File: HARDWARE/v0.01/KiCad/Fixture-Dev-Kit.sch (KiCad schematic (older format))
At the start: 0 parts

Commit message: adding some comments for Howie
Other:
- note added: "- Led Part Number (color, size)\n- confirm LED circuit\n- is 1K resistor correct?"
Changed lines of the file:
@@
 LIBS:contrib
 LIBS:valves
+LIBS:FDN337N
 LIBS:Fixture-Dev-Kit-cache
 EELAYER 25 0
@@
 $Descr A4 11693 8268
 encoding utf-8
-Sheet 1 9
+Sheet 1 10
 Title ""
 Date ""
@@
 $EndSheet
 $Sheet
-S 850  750  2800 2200
+S 850  900  2800 2200
 U 59EE6806
 F0 "Fixture Dev Kit - Functional Computer" 60
@@
 $EndSheet
 $Sheet
-S 6300 5050 1150 800
+S 4350 3850 1150 800
 U 59EFF8A7
-F0 "Fixture Dev Kit - Mosfets" 61
-F1 "FixtureDevKit-Mosfet.sch" 61
+F0 "Fixture Dev Kit - PMosfets" 61
+F1 "FixtureDevKit-PMosfet.sch" 61
 $EndSheet
 $Comp
@@
 Wire Wire Line
 	1300 7350 1300 7450
+Text Notes 8200 4900 0    60   ~ 0
+- Led Part Number (color, size)\n- confirm LED circuit\n- is 1K resistor correct?
+$Sheet
+S 4350 4950 1150 750
+U 59F1138D
+F0 "Fixture Dev Kits - NMosfets" 60
+F1 "FixtureDevKit-NMosfets.sch" 60
+$EndSheet
 $EndSCHEMATC

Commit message: updating the cover page
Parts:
- added J?: POWER, symbol Screw_Terminal_01x02
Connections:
- net labels added: +5V
- net labels removed: VCC
- wire segments 2 -> 5
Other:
- note added: "5V-10A Power Supply\n"
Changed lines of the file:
@@
 $EndDescr
 $Sheet
-S 8100 4550 2400 1200
+S 4050 5300 1700 700
 U 59EE3928
 F0 "Fixture Dev Kit Switches" 60
@@
 $EndSheet
 $Sheet
-S 4750 750  1100 2600
+S 4054 2346 800  1050
 U 59EE50B5
 F0 "Fixture Dev Kit - INA" 60
 F1 "FixtureDevKit-INA.sch" 60
+F2 "I2C-SDA" B T 4704 2346 60
+F3 "I2C-SCK" B T 4554 2346 60
+F4 "C4-VCC-3V3" I T 4254 2346 60
 $EndSheet
 $Sheet
-S 6200 750  1000 2600
+S 5116 2334 784  1066
 U 59EEAF92
 F0 "Fixture Dev Kit - ADS" 60
 F1 "FixtureDevKit-ADS.sch" 60
+F2 "I2C-SDA" B T 5766 2334 60
+F3 "I2C-SCK" B T 5616 2334 60
+F4 "C4-VCC-3V3" I T 5300 2334 60
 $EndSheet
 $Sheet
-S 7700 750  950  2600
+S 4050 3600 800  600
 U 59EE63FB
 F0 "Fixture Dev Kit Dummy Loads" 60
@@
 $EndSheet
 $Sheet
-S 850  900  2800 2200
-U 59EE6806
-F0 "Fixture Dev Kit - Functional Computer" 60
-F1 "FixtureDevKit-Functional-Computer.sch" 60
-$EndSheet
-$Sheet
-S 9300 900  1800 1150
+S 7500 950  1650 1350
 U 59EE1B11
 F0 "Fixture Dev Kit - DUT" 60
@@
 $EndSheet
 $Sheet
-S 6200 3750 1150 850
+S 6205 2345 745  1055
 U 59EF8AA8
 F0 "Fixture Dev Kit - IO Expander" 60
 F1 "FixtureDevKit-IOExpander.sch" 60
+F2 "I2C-SDA" B T 6755 2345 60
+F3 "I2C-SDK" B T 6605 2345 60
+F4 "C4-VCC-4V4" I T 6305 2345 60
 $EndSheet
 $Sheet
-S 4350 3850 1150 800
+S 5850 3600 800  600
 U 59EFF8A7
 F0 "Fixture Dev Kit - PMosfets" 61
@@
 L PWR_FLAG #FLG01
 U 1 1 59EFDEB7
-P 800 7350
-F 0 "#FLG01" H 800 7425 50  0001 C CNN
-F 1 "PWR_FLAG" H 800 7500 50  0000 C CNN
-F 2 "" H 800 7350 50  0001 C CNN
-F 3 "" H 800 7350 50  0001 C CNN
-	1    800  7350
+P 900 7400
+F 0 "#FLG01" H 900 7475 50  0001 C CNN
+F 1 "PWR_FLAG" H 900 7550 50  0000 C CNN
+F 2 "" H 900 7400 50  0001 C CNN
+F 3 "" H 900 7400 50  0001 C CNN
+	1    900  7400
 	1    0    0    -1
 $EndComp
@@
 L PWR_FLAG #FLG02
 U 1 1 59EFDEC9
-P 1300 7350
-F 0 "#FLG02" H 1300 7425 50  0001 C CNN
-F 1 "PWR_FLAG" H 1300 7500 50  0000 C CNN
-F 2 "" H 1300 7350 50  0001 C CNN
-F 3 "" H 1300 7350 50  0001 C CNN
-	1    1300 7350
+P 1400 7400
+F 0 "#FLG02" H 1400 7475 50  0001 C CNN
+F 1 "PWR_FLAG" H 1400 7550 50  0000 C CNN
+F 2 "" H 1400 7400 50  0001 C CNN
+F 3 "" H 1400 7400 50  0001 C CNN
+	1    1400 7400
 	1    0    0    -1
 $EndComp
@@
 L GND #PWR03
 U 1 1 59EFDED6
-P 1300 7450
-F 0 "#PWR03" H 1300 7200 50  0001 C CNN
-F 1 "GND" H 1300 7300 50  0000 C CNN
-F 2 "" H 1300 7450 50  0001 C CNN
-F 3 "" H 1300 7450 50  0001 C CNN
-	1    1300 7450
+P 1400 7500
+F 0 "#PWR03" H 1400 7250 50  0001 C CNN
+F 1 "GND" H 1400 7350 50  0000 C CNN
+F 2 "" H 1400 7500 50  0001 C CNN
+F 3 "" H 1400 7500 50  0001 C CNN
+	1    1400 7500
 	1    0    0    -1
 $EndComp
-$Comp
-L VCC #PWR04
-U 1 1 59EFDEEA
-P 800 7450
-F 0 "#PWR04" H 800 7300 50  0001 C CNN
-F 1 "VCC" H 800 7600 50  0000 C CNN
-F 2 "" H 800 7450 50  0001 C CNN
-F 3 "" H 800 7450 50  0001 C CNN
-	1    800  7450
-	-1   0    0    1
-$EndComp
 Wire Wire Line
-	800  7350 800  7450
+	900  7400 900  7500
 Wire Wire Line
-	1300 7350 1300 7450
-Text Notes 8200 4900 0    60   ~ 0
-- Led Part Number (color, size)\n- confirm LED circuit\n- is 1K resistor correct?
+	1400 7400 1400 7500
 $Sheet
-S 4350 4950 1150 750
+S 5850 4500 800  600
 U 59F1138D
 F0 "Fixture Dev Kits - NMosfets" 60
 F1 "FixtureDevKit-NMosfets.sch" 60
 $EndSheet
+$Comp
+L Screw_Terminal_01x02 J?
+U 1 1 59F1B009
+P 1050 6850
+F 0 "J?" H 1050 6950 50  0000 C CNN
+F 1 "POWER" H 1050 6650 50  0000 C CNN
+F 2 "" H 1050 6850 50  0001 C CNN
+F 3 "" H 1050 6850 50  0001 C CNN
+	1    1050 6850
+	-1   0    0    1
+$EndComp
+Wire Wire Line
+	1250 6750 1500 6750
+$Comp
+L GND #PWR?
+U 1 1 59F1B0B1
+P 1500 6850
+F 0 "#PWR?" H 1500 6600 50  0001 C CNN
+F 1 "GND" H 1500 6700 50  0000 C CNN
+F 2 "" H 1500 6850 50  0001 C CNN
+F 3 "" H 1500 6850 50  0001 C CNN
+	1    1500 6850
+	1    0    0    -1
+$EndComp
+Wire Wire Line
+	1250 6850 1500 6850
+Text Notes 600  6350 0    98   ~ 0
+5V-10A Power Supply\n
+Wire Notes Line
+	550  6150 2250 6150
+Wire Notes Line
+	2250 6150 2250 7150
+Wire Notes Line
+	2250 7150 550  7150
+Wire Notes Line
+	550  7150 550  6150
+Wire Notes Line
+	550  6400 2250 6400
+$Comp
+L +5V #PWR?
+U 1 1 59F1DD6A
+P 900 7500
+F 0 "#PWR?" H 900 7350 50  0001 C CNN
+F 1 "+5V" H 900 7640 50  0000 C CNN
+F 2 "" H 900 7500 50  0001 C CNN
+F 3 "" H 900 7500 50  0001 C CNN
+	1    900  7500
+	-1   0    0    1
+$EndComp
+$Comp
+L +5V #PWR?
+U 1 1 59F1DD81
+P 1500 6750
+F 0 "#PWR?" H 1500 6600 50  0001 C CNN
+F 1 "+5V" H 1500 6890 50  0000 C CNN
+F 2 "" H 1500 6750 50  0001 C CNN
+F 3 "" H 1500 6750 50  0001 C CNN
+	1    1500 6750
+	1    0    0    -1
+$EndComp
+$Sheet
+S 1500 950  1650 1350
+U 59EE6806
+F0 "Fixture Dev Kit - Functional Computer" 60
+F1 "FixtureDevKit-Functional-Computer.sch" 60
+F2 "I2C-SDA" B R 3150 1150 60
+F3 "I2C-SCK" B R 3150 1250 60
+F4 "+5V" I R 3150 1600 60
+F5 "C4-VCC-5V" O R 3150 1900 60
+F6 "C4-VCC-3V3" O R 3150 2050 60
+$EndSheet
+$Comp
+L +5V #PWR?
+U 1 1 59F2758A
+P 3300 1600
+F 0 "#PWR?" H 3300 1450 50  0001 C CNN
+F 1 "+5V" H 3300 1740 50  0000 C CNN
+F 2 "" H 3300 1600 50  0001 C CNN
+F 3 "" H 3300 1600 50  0001 C CNN
+	1    3300 1600
+	0    1    1    0
+$EndComp
+Wire Wire Line
+	3300 1600 3150 1600
+Text Notes 4100 5650 0    60   ~ 0
+- Led Part Number (color, size)\n- confirm LED circuit\n- is 1K resistor correct?
 $EndSCHEMATC

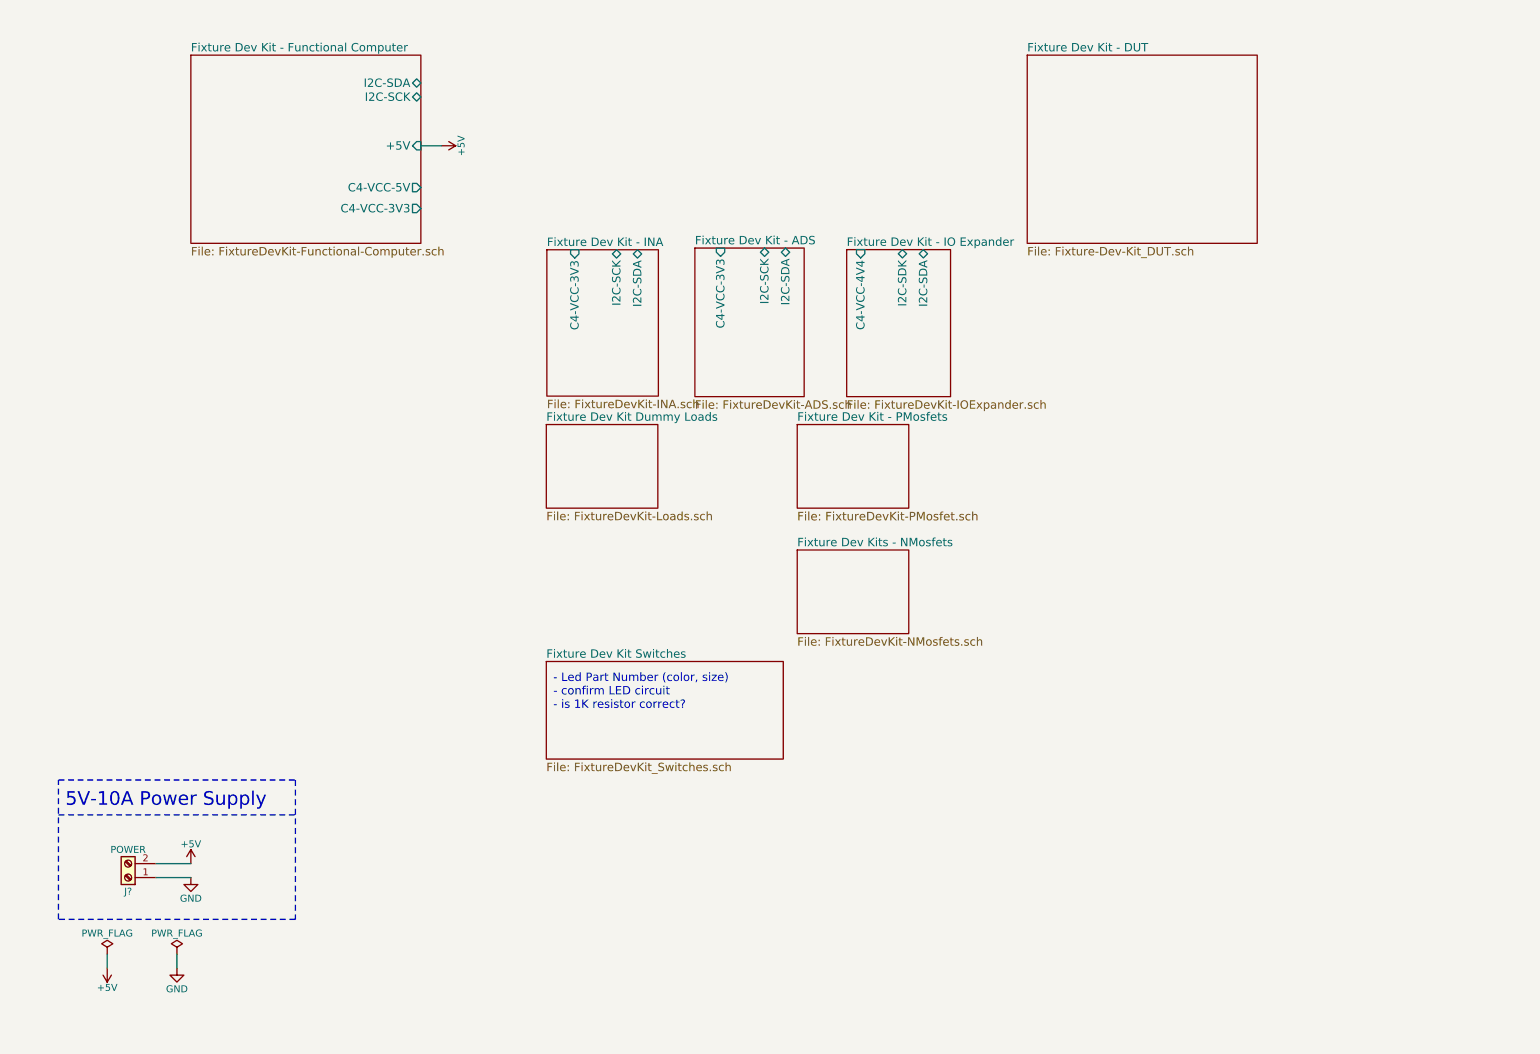
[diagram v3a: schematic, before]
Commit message: adjusting page sizes and cleaning up schematics
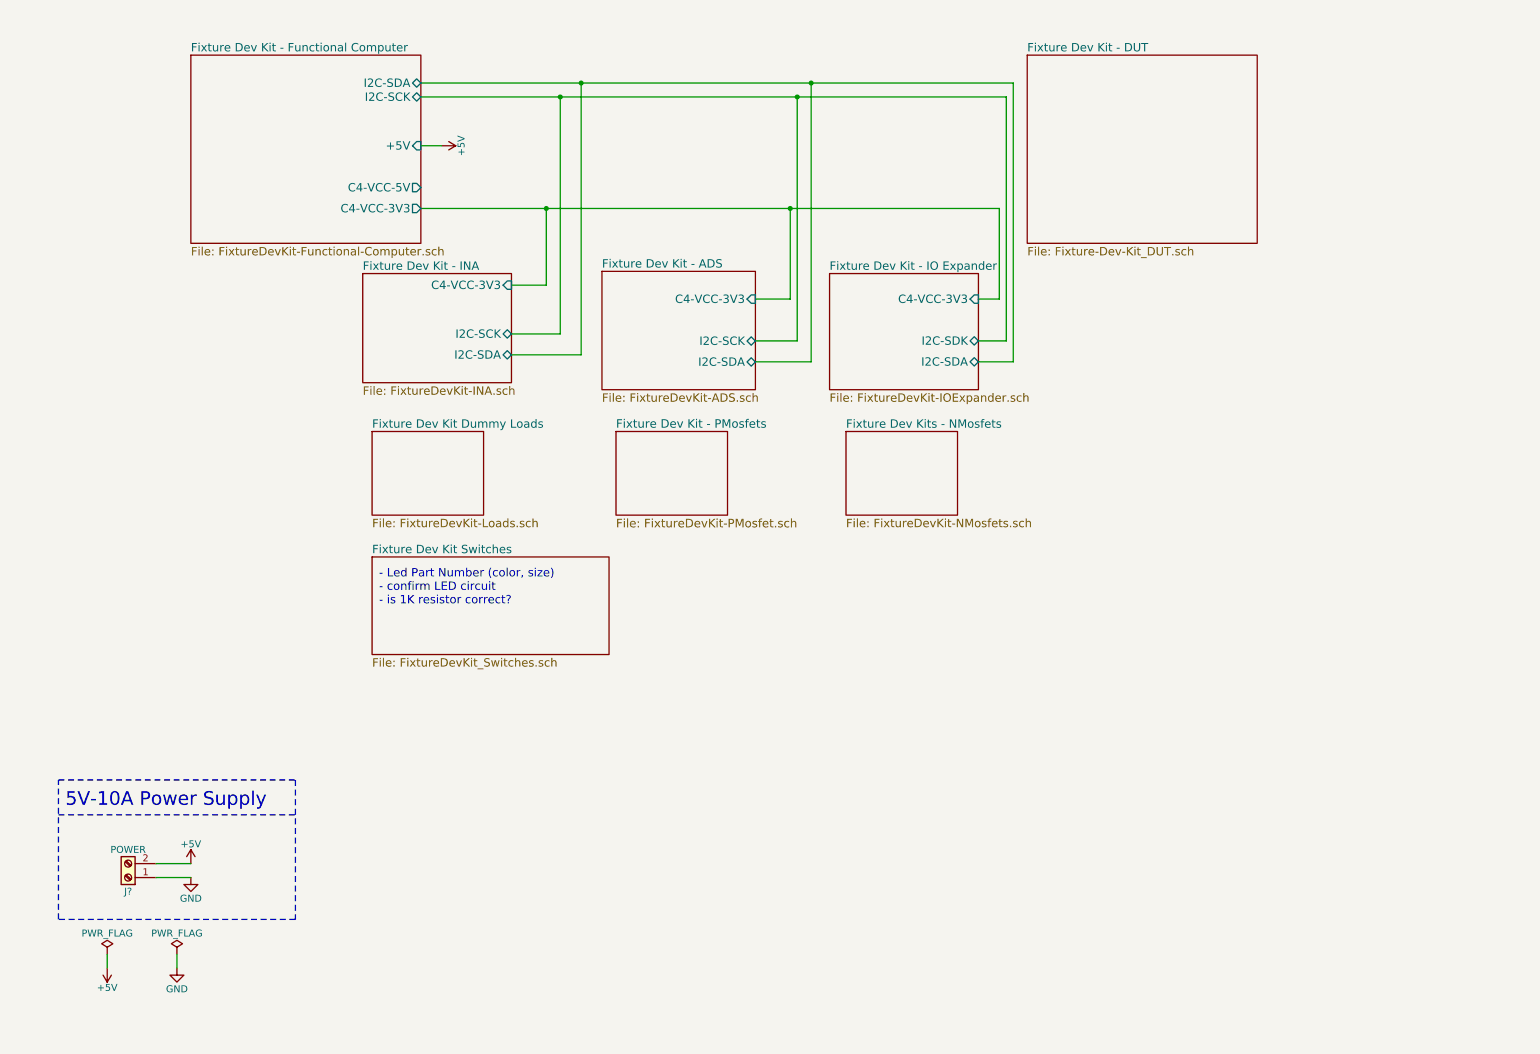
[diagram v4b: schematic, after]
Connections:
- wire segments 5 -> 26
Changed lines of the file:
@@
 EELAYER 25 0
 EELAYER END
-$Descr A4 11693 8268
+$Descr USLetter 11000 8500
 encoding utf-8
 Sheet 1 10
@@
 $EndDescr
 $Sheet
-S 4050 5300 1700 700
+S 2800 4550 1700 700
 U 59EE3928
 F0 "Fixture Dev Kit Switches" 60
@@
 $EndSheet
 $Sheet
-S 4054 2346 800  1050
-U 59EE50B5
-F0 "Fixture Dev Kit - INA" 60
-F1 "FixtureDevKit-INA.sch" 60
-F2 "I2C-SDA" B T 4704 2346 60
-F3 "I2C-SCK" B T 4554 2346 60
-F4 "C4-VCC-3V3" I T 4254 2346 60
-$EndSheet
-$Sheet
-S 5116 2334 784  1066
+S 4449 2501 1101 849
 U 59EEAF92
 F0 "Fixture Dev Kit - ADS" 60
 F1 "FixtureDevKit-ADS.sch" 60
-F2 "I2C-SDA" B T 5766 2334 60
-F3 "I2C-SCK" B T 5616 2334 60
-F4 "C4-VCC-3V3" I T 5300 2334 60
-$EndSheet
-$Sheet
-S 4050 3600 800  600
+F2 "I2C-SDA" B R 5550 3151 60
+F3 "I2C-SCK" B R 5550 3001 60
+F4 "C4-VCC-3V3" I R 5550 2700 60
+$EndSheet
+$Sheet
+S 2800 3650 800  600
 U 59EE63FB
 F0 "Fixture Dev Kit Dummy Loads" 60
@@
 $EndSheet
 $Sheet
-S 6205 2345 745  1055
+S 6082 2517 1068 833
 U 59EF8AA8
 F0 "Fixture Dev Kit - IO Expander" 60
 F1 "FixtureDevKit-IOExpander.sch" 60
-F2 "I2C-SDA" B T 6755 2345 60
-F3 "I2C-SDK" B T 6605 2345 60
-F4 "C4-VCC-4V4" I T 6305 2345 60
-$EndSheet
-$Sheet
-S 5850 3600 800  600
+F2 "I2C-SDA" B R 7150 3150 60
+F3 "I2C-SDK" B R 7150 3000 60
+F4 "C4-VCC-3V3" I R 7150 2700 60
+$EndSheet
+$Sheet
+S 4550 3650 800  600
 U 59EFF8A7
 F0 "Fixture Dev Kit - PMosfets" 61
@@
 	1400 7400 1400 7500
 $Sheet
-S 5850 4500 800  600
+S 6200 3650 800  600
 U 59F1138D
 F0 "Fixture Dev Kits - NMosfets" 60
@@
 Wire Wire Line
 	3300 1600 3150 1600
-Text Notes 4100 5650 0    60   ~ 0
+Text Notes 2850 4900 0    60   ~ 0
 - Led Part Number (color, size)\n- confirm LED circuit\n- is 1K resistor correct?
+$Sheet
+S 2733 2517 1067 783
+U 59EE50B5
+F0 "Fixture Dev Kit - INA" 60
+F1 "FixtureDevKit-INA.sch" 60
+F2 "I2C-SDA" B R 3800 3100 60
+F3 "I2C-SCK" B R 3800 2950 60
+F4 "C4-VCC-3V3" I R 3800 2600 60
+$EndSheet
+Wire Wire Line
+	3800 2600 4050 2600
+Wire Wire Line
+	4050 2600 4050 2050
+Wire Wire Line
+	3150 2050 7300 2050
+Wire Wire Line
+	3800 2950 4150 2950
+Wire Wire Line
+	4150 2950 4150 1250
+Wire Wire Line
+	3150 1250 7350 1250
+Wire Wire Line
+	3800 3100 4300 3100
+Wire Wire Line
+	4300 3100 4300 1150
+Wire Wire Line
+	3150 1150 7400 1150
+Wire Wire Line
+	5800 2050 5800 2700
+Wire Wire Line
+	5800 2700 5550 2700
+Connection ~ 4050 2050
+Wire Wire Line
+	5550 3000 5850 3000
+Wire Wire Line
+	5850 3000 5850 1250
+Connection ~ 4150 1250
+Wire Wire Line
+	5550 3150 5950 3150
+Wire Wire Line
+	5950 3150 5950 1150
+Connection ~ 4300 1150
+Wire Wire Line
+	7300 2050 7300 2700
+Wire Wire Line
+	7300 2700 7150 2700
+Connection ~ 5800 2050
+Wire Wire Line
+	7150 3000 7350 3000
+Wire Wire Line
+	7350 3000 7350 1250
+Connection ~ 5850 1250
+Wire Wire Line
+	7150 3150 7400 3150
+Wire Wire Line
+	7400 3150 7400 1150
+Connection ~ 5950 1150
 $EndSCHEMATC

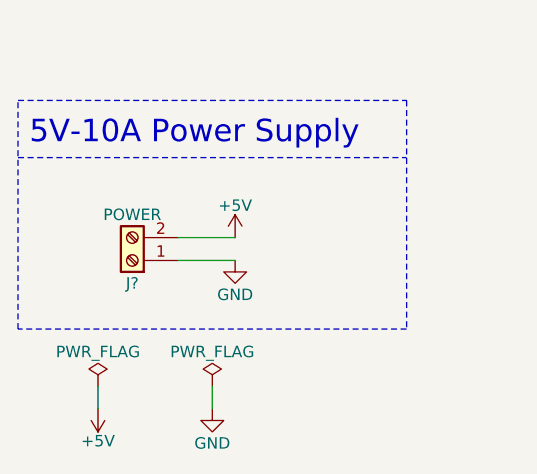
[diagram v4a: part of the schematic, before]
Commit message: cleaning up schematic, run rules check, generate net list
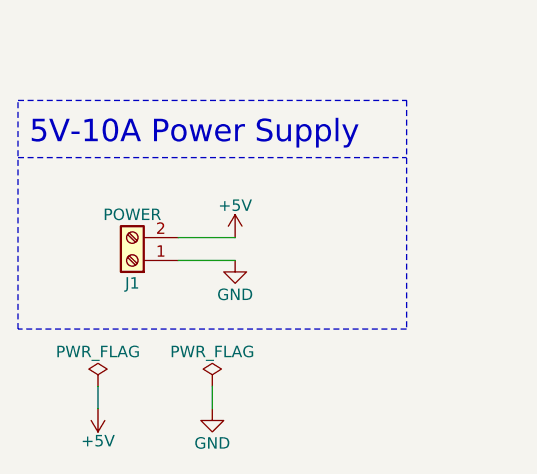
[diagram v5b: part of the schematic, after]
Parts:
- gave numbers to parts that had none: 1
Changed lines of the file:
@@
 $EndSheet
 $Comp
-L Screw_Terminal_01x02 J?
+L Screw_Terminal_01x02 J1
 U 1 1 59F1B009
 P 1050 6850
-F 0 "J?" H 1050 6950 50  0000 C CNN
+F 0 "J1" H 1050 6950 50  0000 C CNN
 F 1 "POWER" H 1050 6650 50  0000 C CNN
 F 2 "" H 1050 6850 50  0001 C CNN
@@
 	1250 6750 1500 6750
 $Comp
-L GND #PWR?
+L GND #PWR04
 U 1 1 59F1B0B1
 P 1500 6850
-F 0 "#PWR?" H 1500 6600 50  0001 C CNN
+F 0 "#PWR04" H 1500 6600 50  0001 C CNN
 F 1 "GND" H 1500 6700 50  0000 C CNN
 F 2 "" H 1500 6850 50  0001 C CNN
@@
 	550  6400 2250 6400
 $Comp
-L +5V #PWR?
+L +5V #PWR05
 U 1 1 59F1DD6A
 P 900 7500
-F 0 "#PWR?" H 900 7350 50  0001 C CNN
+F 0 "#PWR05" H 900 7350 50  0001 C CNN
 F 1 "+5V" H 900 7640 50  0000 C CNN
 F 2 "" H 900 7500 50  0001 C CNN
@@
 $EndComp
 $Comp
-L +5V #PWR?
+L +5V #PWR06
 U 1 1 59F1DD81
 P 1500 6750
-F 0 "#PWR?" H 1500 6600 50  0001 C CNN
+F 0 "#PWR06" H 1500 6600 50  0001 C CNN
 F 1 "+5V" H 1500 6890 50  0000 C CNN
 F 2 "" H 1500 6750 50  0001 C CNN
@@
 $EndSheet
 $Comp
-L +5V #PWR?
+L +5V #PWR07
 U 1 1 59F2758A
 P 3300 1600
-F 0 "#PWR?" H 3300 1450 50  0001 C CNN
+F 0 "#PWR07" H 3300 1450 50  0001 C CNN
 F 1 "+5V" H 3300 1740 50  0000 C CNN
 F 2 "" H 3300 1600 50  0001 C CNN

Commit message: adding footprints
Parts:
- J1: footprint (none) -> TerminalBlocks_Phoenix:TerminalBlock_Phoenix_MPT-2.54mm_2pol
